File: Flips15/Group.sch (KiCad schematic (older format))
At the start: 6 parts, among them U301 74238, U302 ULN2803/2003, U303 74238, U304 TD62783

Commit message: adding support for optional COM pin at BRDIC1
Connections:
- net GND: no longer U302.1 (I1), U304.1 (I1)
- new net CTLCOMH: U304.1 (I1)
- new net CTLCOML: U302.1 (I1)
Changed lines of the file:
@@
 AR Path="/5C4DA960/5C4DAAA8/5C4CE34D" Ref="U1004"  Part="1"
 AR Path="/5C4DA960/5C4DAABF/5C4CE34D" Ref="U1104"  Part="1"
-F 0 "U804" H 5900 4978 50  0000 C CNN
+F 0 "U1104" H 5900 4978 50  0000 C CNN
 F 1 "TD62783" H 5900 4887 50  0000 C CNN
 F 2 "Housings_DIP:DIP-18_W7.62mm_Socket" H 5900 3750 50  0001 C CNN
@@
 AR Path="/5C4DA960/5C4DAAA8/5C4CE354" Ref="U1001"  Part="1"
 AR Path="/5C4DA960/5C4DAABF/5C4CE354" Ref="U1101"  Part="1"
-F 0 "U801" H 4550 2116 50  0000 C CNN
+F 0 "U1101" H 4550 2116 50  0000 C CNN
 F 1 "74238" H 4550 2025 50  0000 C CNN
 F 2 "Housings_SOIC:SOIC-16_3.9x9.9mm_Pitch1.27mm" H 4550 1600 50  0001 C CNN
@@
 AR Path="/5C4DA960/5C4DAAA8/5C4CE35B" Ref="U1003"  Part="1"
 AR Path="/5C4DA960/5C4DAABF/5C4CE35B" Ref="U1103"  Part="1"
-F 0 "U803" H 4550 4716 50  0000 C CNN
+F 0 "U1103" H 4550 4716 50  0000 C CNN
 F 1 "74238" H 4550 4625 50  0000 C CNN
 F 2 "Housings_SOIC:SOIC-16_3.9x9.9mm_Pitch1.27mm" H 4550 4200 50  0001 C CNN
@@
 AR Path="/5C4DA960/5C4DAAA8/5C4D1DBE" Ref="#PWR01006"  Part="1"
 AR Path="/5C4DA960/5C4DAABF/5C4D1DBE" Ref="#PWR01106"  Part="1"
-F 0 "#PWR0806" H 5900 2350 50  0001 C CNN
+F 0 "#PWR01106" H 5900 2350 50  0001 C CNN
 F 1 "GND" H 5905 2427 50  0000 C CNN
 F 2 "" H 5900 2600 50  0001 C CNN
@@
 AR Path="/5C4DA960/5C4DAAA8/5C4D1DFA" Ref="#PWR01012"  Part="1"
 AR Path="/5C4DA960/5C4DAABF/5C4D1DFA" Ref="#PWR01112"  Part="1"
-F 0 "#PWR0812" H 5900 5050 50  0001 C CNN
+F 0 "#PWR01112" H 5900 5050 50  0001 C CNN
 F 1 "GND" H 5905 5127 50  0000 C CNN
 F 2 "" H 5900 5300 50  0001 C CNN
@@
 AR Path="/5C4DA960/5C4DAAA8/5C4D1E20" Ref="#PWR01011"  Part="1"
 AR Path="/5C4DA960/5C4DAABF/5C4D1E20" Ref="#PWR01111"  Part="1"
-F 0 "#PWR0811" H 4550 5050 50  0001 C CNN
+F 0 "#PWR01111" H 4550 5050 50  0001 C CNN
 F 1 "GND" H 4555 5127 50  0000 C CNN
 F 2 "" H 4550 5300 50  0001 C CNN
@@
 AR Path="/5C4DA960/5C4DAAA8/5C4D1E50" Ref="#PWR01005"  Part="1"
 AR Path="/5C4DA960/5C4DAABF/5C4D1E50" Ref="#PWR01105"  Part="1"
-F 0 "#PWR0805" H 4550 2350 50  0001 C CNN
+F 0 "#PWR01105" H 4550 2350 50  0001 C CNN
 F 1 "GND" H 4555 2427 50  0000 C CNN
 F 2 "" H 4550 2600 50  0001 C CNN
@@
 AR Path="/5C4DA960/5C4DAAA8/5C4D1F03" Ref="#PWR01002"  Part="1"
 AR Path="/5C4DA960/5C4DAABF/5C4D1F03" Ref="#PWR01102"  Part="1"
-F 0 "#PWR0802" H 6400 600 50  0001 C CNN
+F 0 "#PWR01102" H 6400 600 50  0001 C CNN
 F 1 "+24V" H 6415 923 50  0000 C CNN
 F 2 "" H 6400 750 50  0001 C CNN
@@
 AR Path="/5C4DA960/5C4DAAA8/5C4D1F1D" Ref="#PWR01008"  Part="1"
 AR Path="/5C4DA960/5C4DAABF/5C4D1F1D" Ref="#PWR01108"  Part="1"
-F 0 "#PWR0808" H 5900 3250 50  0001 C CNN
+F 0 "#PWR01108" H 5900 3250 50  0001 C CNN
 F 1 "+24V" H 5915 3573 50  0000 C CNN
 F 2 "" H 5900 3400 50  0001 C CNN
@@
 AR Path="/5C4DA960/5C4DAAA8/5C4D1FAA" Ref="#PWR01001"  Part="1"
 AR Path="/5C4DA960/5C4DAABF/5C4D1FAA" Ref="#PWR01101"  Part="1"
-F 0 "#PWR0801" H 4550 600 50  0001 C CNN
+F 0 "#PWR01101" H 4550 600 50  0001 C CNN
 F 1 "VCC" H 4567 923 50  0000 C CNN
 F 2 "" H 4550 750 50  0001 C CNN
@@
 AR Path="/5C4DA960/5C4DAAA8/5C4D1FD4" Ref="#PWR01007"  Part="1"
 AR Path="/5C4DA960/5C4DAABF/5C4D1FD4" Ref="#PWR01107"  Part="1"
-F 0 "#PWR0807" H 4550 3250 50  0001 C CNN
+F 0 "#PWR01107" H 4550 3250 50  0001 C CNN
 F 1 "VCC" H 4567 3573 50  0000 C CNN
 F 2 "" H 4550 3400 50  0001 C CNN
@@
 AR Path="/5C4DA960/5C4DAAA8/5C4DA0A7" Ref="#PWR01010"  Part="1"
 AR Path="/5C4DA960/5C4DAABF/5C4DA0A7" Ref="#PWR01110"  Part="1"
-F 0 "#PWR0810" H 3900 3900 50  0001 C CNN
+F 0 "#PWR01110" H 3900 3900 50  0001 C CNN
 F 1 "GND" V 3905 4022 50  0000 R CNN
 F 2 "" H 3900 4150 50  0001 C CNN
@@
 AR Path="/5C4DA960/5C4DAAA8/5C4E1AEA" Ref="U1002"  Part="1"
 AR Path="/5C4DA960/5C4DAABF/5C4E1AEA" Ref="U1102"  Part="1"
-F 0 "U802" H 5900 2167 50  0000 C CNN
+F 0 "U1102" H 5900 2167 50  0000 C CNN
 F 1 "ULN2803/2003" H 5900 2076 50  0000 C CNN
 F 2 "Housings_DIP:DIP-18_W7.62mm_Socket" H 5950 950 50  0001 L CNN
@@
 AR Path="/5C4DA960/5C4DAAA8/5C4F67EE" Ref="C1002"  Part="1"
 AR Path="/5C4DA960/5C4DAABF/5C4F67EE" Ref="C1102"  Part="1"
-F 0 "C802" V 4021 3500 50  0000 C CNN
+F 0 "C1102" V 4021 3500 50  0000 C CNN
 F 1 "0μ1" V 4112 3500 50  0000 C CNN
 F 2 "Capacitors_SMD:C_0805_HandSoldering" H 4250 3500 50  0001 C CNN
@@
 AR Path="/5C4DA960/5C4DAAA8/5C4F6885" Ref="C1001"  Part="1"
 AR Path="/5C4DA960/5C4DAABF/5C4F6885" Ref="C1101"  Part="1"
-F 0 "C801" V 4021 850 50  0000 C CNN
+F 0 "C1101" V 4021 850 50  0000 C CNN
 F 1 "0μ1" V 4112 850 50  0000 C CNN
 F 2 "Capacitors_SMD:C_0805_HandSoldering" H 4250 850 50  0001 C CNN
@@
 AR Path="/5C4DA960/5C4DAAA8/5C4F6943" Ref="#PWR01003"  Part="1"
 AR Path="/5C4DA960/5C4DAABF/5C4F6943" Ref="#PWR01103"  Part="1"
-F 0 "#PWR0803" H 3900 600 50  0001 C CNN
+F 0 "#PWR01103" H 3900 600 50  0001 C CNN
 F 1 "GND" V 3905 722 50  0000 R CNN
 F 2 "" H 3900 850 50  0001 C CNN
@@
 AR Path="/5C4DA960/5C4DAAA8/5C4F6978" Ref="#PWR01009"  Part="1"
 AR Path="/5C4DA960/5C4DAABF/5C4F6978" Ref="#PWR01109"  Part="1"
-F 0 "#PWR0809" H 3900 3250 50  0001 C CNN
+F 0 "#PWR01109" H 3900 3250 50  0001 C CNN
 F 1 "GND" V 3905 3372 50  0000 R CNN
 F 2 "" H 3900 3500 50  0001 C CNN
@@
 AR Path="/5C4DA960/5C4DAAA8/5C4EB0F4" Ref="#PWR0130"  Part="1"
 AR Path="/5C4DA960/5C4DAABF/5C4EB0F4" Ref="#PWR0133"  Part="1"
-F 0 "#PWR0124" H 3900 3750 50  0001 C CNN
+F 0 "#PWR0133" H 3900 3750 50  0001 C CNN
 F 1 "GND" V 3905 3872 50  0000 R CNN
 F 2 "" H 3900 4000 50  0001 C CNN
@@
 AR Path="/5C4DA960/5C4DAAA8/5C4EC62E" Ref="#PWR0131"  Part="1"
 AR Path="/5C4DA960/5C4DAABF/5C4EC62E" Ref="#PWR0134"  Part="1"
-F 0 "#PWR0125" H 3900 1150 50  0001 C CNN
+F 0 "#PWR0134" H 3900 1150 50  0001 C CNN
 F 1 "GND" V 3905 1272 50  0000 R CNN
 F 2 "" H 3900 1400 50  0001 C CNN
@@
 AR Path="/5C4DA960/5C4DAAA8/5C4EC645" Ref="#PWR0132"  Part="1"
 AR Path="/5C4DA960/5C4DAABF/5C4EC645" Ref="#PWR0135"  Part="1"
-F 0 "#PWR0126" H 3900 1300 50  0001 C CNN
+F 0 "#PWR0135" H 3900 1300 50  0001 C CNN
 F 1 "GND" V 3905 1422 50  0000 R CNN
 F 2 "" H 3900 1550 50  0001 C CNN
@@
 NoConn ~ 5100 1400
 NoConn ~ 5100 4000
-$Comp
-L power:GND #PWR?
-U 1 1 5C57C882
-P 5500 1400
-AR Path="/5C4DA960/5C4DAA7A/5C57C882" Ref="#PWR?"  Part="1"
-AR Path="/5C4DA960/5C4DAA91/5C57C882" Ref="#PWR?"  Part="1"
-AR Path="/5C4DA960/5C4DAAA8/5C57C882" Ref="#PWR?"  Part="1"
-AR Path="/5C4DA960/5C4DAABF/5C57C882" Ref="#PWR?"  Part="1"
-F 0 "#PWR?" H 5500 1150 50  0001 C CNN
-F 1 "GND" V 5505 1272 50  0000 R CNN
-F 2 "" H 5500 1400 50  0001 C CNN
-F 3 "" H 5500 1400 50  0001 C CNN
-	1    5500 1400
-	0    1    1    0
-$EndComp
-$Comp
-L power:GND #PWR?
-U 1 1 5C57C8A6
-P 5500 4000
-AR Path="/5C4DA960/5C4DAA7A/5C57C8A6" Ref="#PWR?"  Part="1"
-AR Path="/5C4DA960/5C4DAA91/5C57C8A6" Ref="#PWR?"  Part="1"
-AR Path="/5C4DA960/5C4DAAA8/5C57C8A6" Ref="#PWR?"  Part="1"
-AR Path="/5C4DA960/5C4DAABF/5C57C8A6" Ref="#PWR?"  Part="1"
-F 0 "#PWR?" H 5500 3750 50  0001 C CNN
-F 1 "GND" V 5505 3872 50  0000 R CNN
-F 2 "" H 5500 4000 50  0001 C CNN
-F 3 "" H 5500 4000 50  0001 C CNN
-	1    5500 4000
-	0    1    1    0
-$EndComp
+Text HLabel 5250 850  0    50   Input ~ 0
+CTLCOML
+Wire Wire Line
+	5500 1400 5400 1400
+Wire Wire Line
+	5400 1400 5400 850
+Wire Wire Line
+	5400 850  5250 850
+Text HLabel 5250 3500 0    50   Input ~ 0
+CTLCOMH
+Wire Wire Line
+	5250 3500 5400 3500
+Wire Wire Line
+	5400 3500 5400 4000
+Wire Wire Line
+	5400 4000 5500 4000
 $EndSCHEMATC

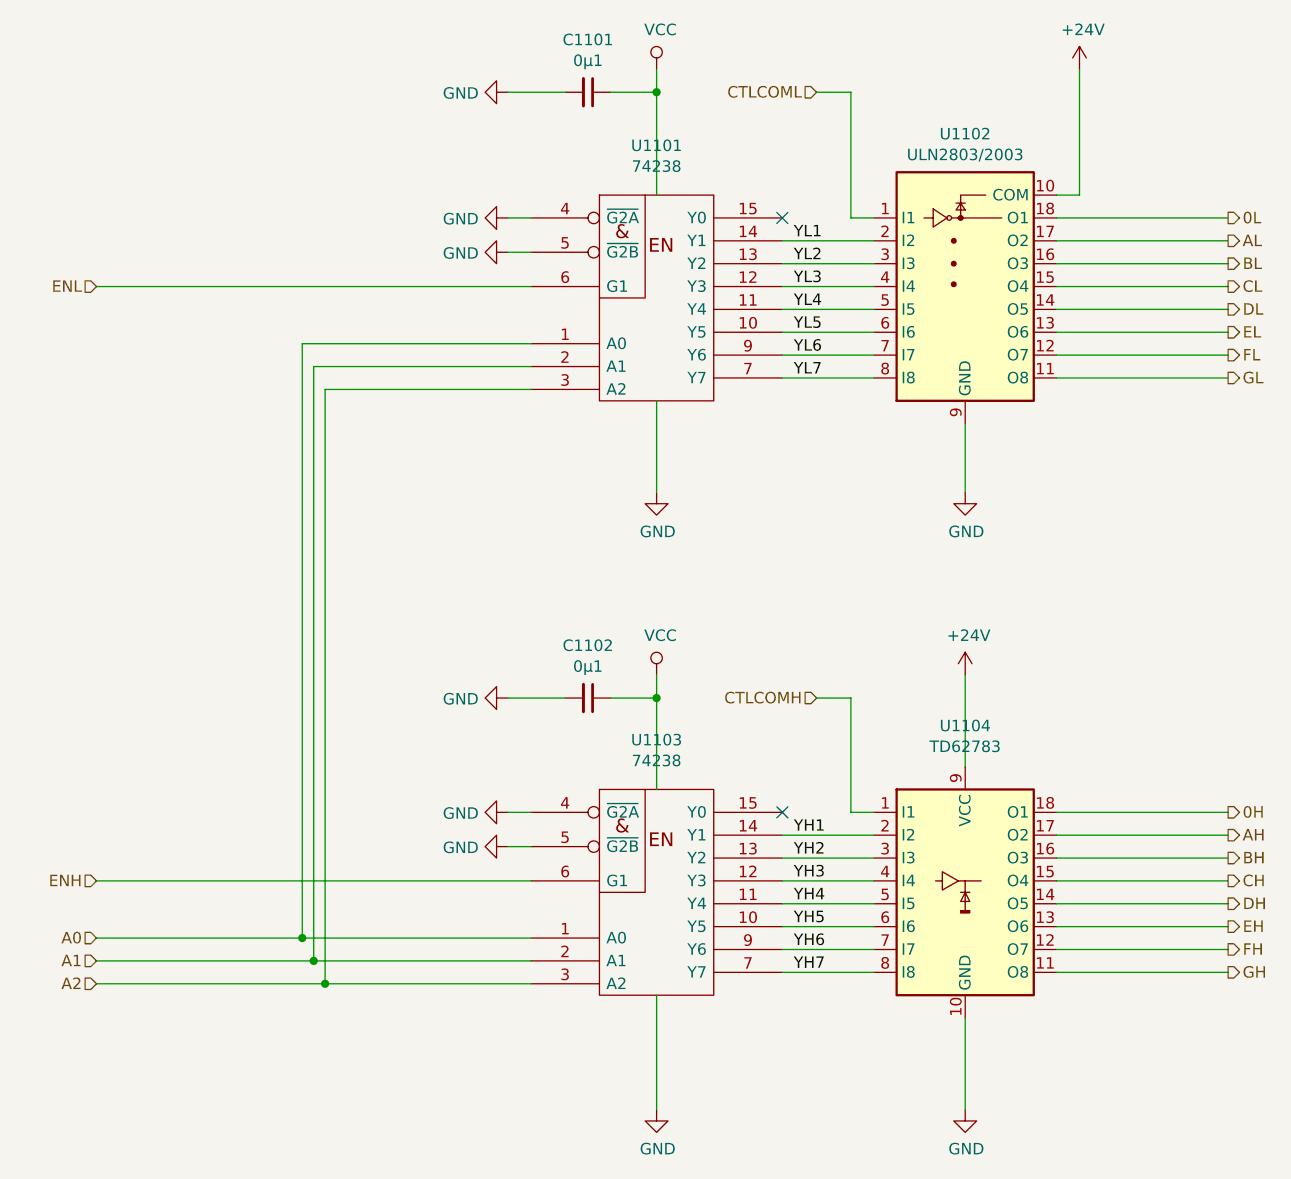
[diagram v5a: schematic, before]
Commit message: re-annotating to get more compact part numbers
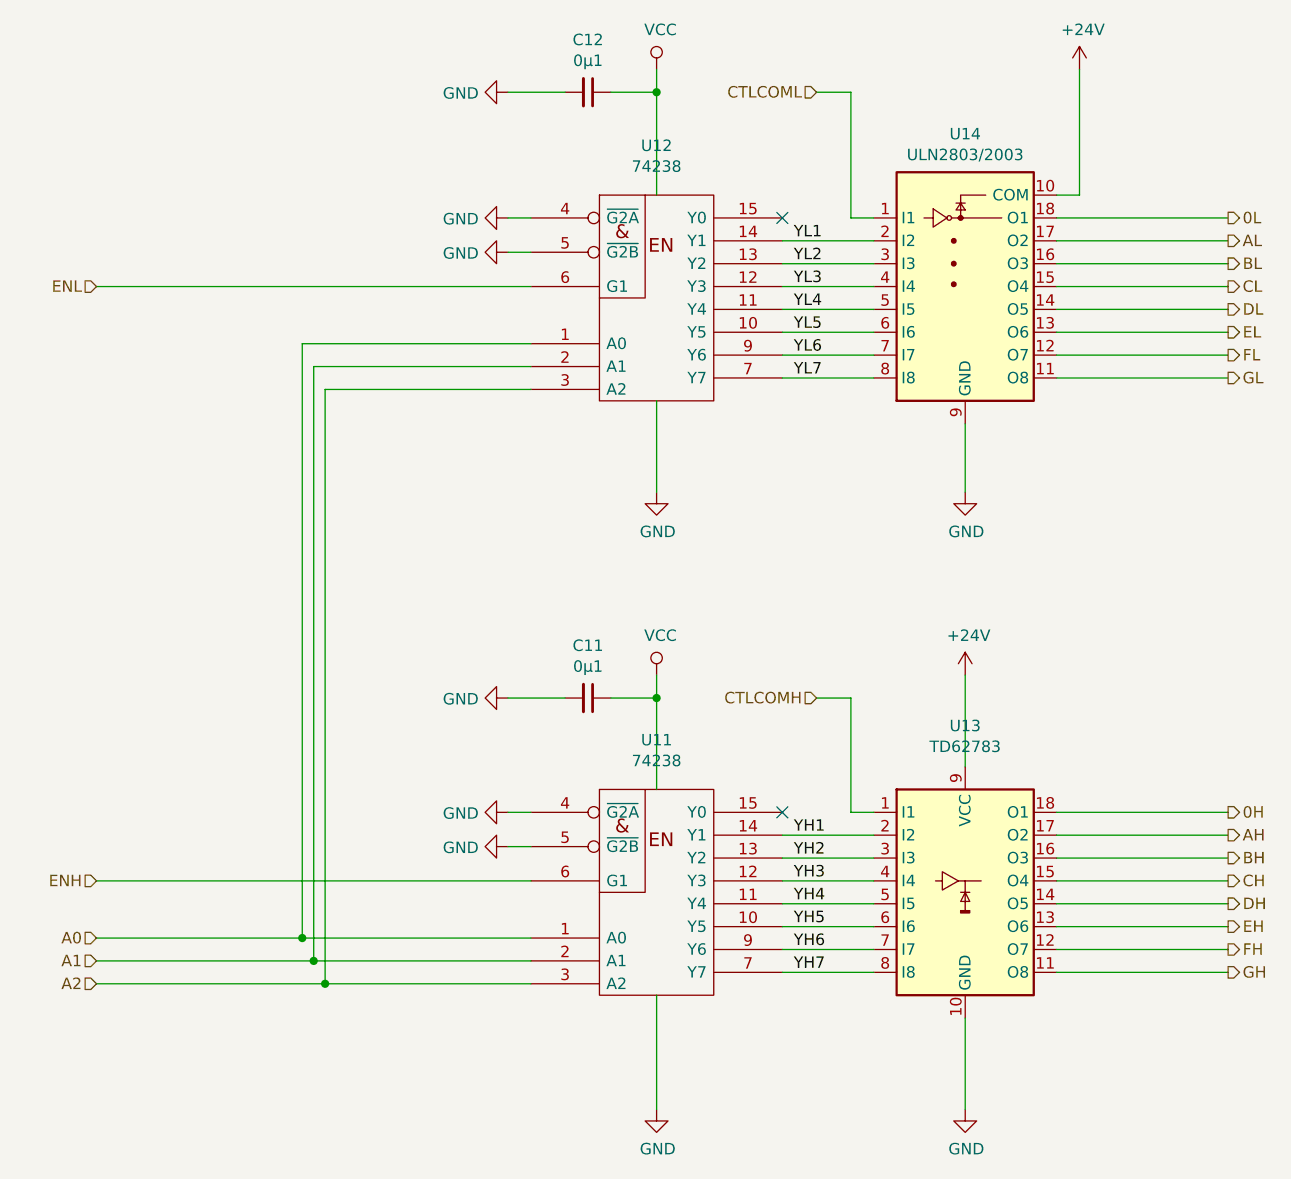
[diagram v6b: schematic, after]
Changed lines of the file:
@@
 AR Path="/5C4DA950/5C4DAAA8/5C4CE34D" Ref="U504"  Part="1"
 AR Path="/5C4DA950/5C4DAABF/5C4CE34D" Ref="U604"  Part="1"
-AR Path="/5C4DA960/5C4DAA7A/5C4CE34D" Ref="U804"  Part="1"
-AR Path="/5C4DA960/5C4DAA91/5C4CE34D" Ref="U904"  Part="1"
-AR Path="/5C4DA960/5C4DAAA8/5C4CE34D" Ref="U1004"  Part="1"
-AR Path="/5C4DA960/5C4DAABF/5C4CE34D" Ref="U1104"  Part="1"
-F 0 "U1104" H 5900 4978 50  0000 C CNN
+AR Path="/5C4DA960/5C4DAA7A/5C4CE34D" Ref="U13"  Part="1"
+AR Path="/5C4DA960/5C4DAA91/5C4CE34D" Ref="U23"  Part="1"
+AR Path="/5C4DA960/5C4DAAA8/5C4CE34D" Ref="U33"  Part="1"
+AR Path="/5C4DA960/5C4DAABF/5C4CE34D" Ref="U43"  Part="1"
+F 0 "U13" H 5900 4978 50  0000 C CNN
 F 1 "TD62783" H 5900 4887 50  0000 C CNN
 F 2 "Housings_DIP:DIP-18_W7.62mm_Socket" H 5900 3750 50  0001 C CNN
@@
 AR Path="/5C4DA950/5C4DAAA8/5C4CE354" Ref="U501"  Part="1"
 AR Path="/5C4DA950/5C4DAABF/5C4CE354" Ref="U601"  Part="1"
-AR Path="/5C4DA960/5C4DAA7A/5C4CE354" Ref="U801"  Part="1"
-AR Path="/5C4DA960/5C4DAA91/5C4CE354" Ref="U901"  Part="1"
-AR Path="/5C4DA960/5C4DAAA8/5C4CE354" Ref="U1001"  Part="1"
-AR Path="/5C4DA960/5C4DAABF/5C4CE354" Ref="U1101"  Part="1"
-F 0 "U1101" H 4550 2116 50  0000 C CNN
+AR Path="/5C4DA960/5C4DAA7A/5C4CE354" Ref="U12"  Part="1"
+AR Path="/5C4DA960/5C4DAA91/5C4CE354" Ref="U22"  Part="1"
+AR Path="/5C4DA960/5C4DAAA8/5C4CE354" Ref="U32"  Part="1"
+AR Path="/5C4DA960/5C4DAABF/5C4CE354" Ref="U42"  Part="1"
+F 0 "U12" H 4550 2116 50  0000 C CNN
 F 1 "74238" H 4550 2025 50  0000 C CNN
 F 2 "Housings_SOIC:SOIC-16_3.9x9.9mm_Pitch1.27mm" H 4550 1600 50  0001 C CNN
@@
 AR Path="/5C4DA950/5C4DAAA8/5C4CE35B" Ref="U503"  Part="1"
 AR Path="/5C4DA950/5C4DAABF/5C4CE35B" Ref="U603"  Part="1"
-AR Path="/5C4DA960/5C4DAA7A/5C4CE35B" Ref="U803"  Part="1"
-AR Path="/5C4DA960/5C4DAA91/5C4CE35B" Ref="U903"  Part="1"
-AR Path="/5C4DA960/5C4DAAA8/5C4CE35B" Ref="U1003"  Part="1"
-AR Path="/5C4DA960/5C4DAABF/5C4CE35B" Ref="U1103"  Part="1"
-F 0 "U1103" H 4550 4716 50  0000 C CNN
+AR Path="/5C4DA960/5C4DAA7A/5C4CE35B" Ref="U11"  Part="1"
+AR Path="/5C4DA960/5C4DAA91/5C4CE35B" Ref="U21"  Part="1"
+AR Path="/5C4DA960/5C4DAAA8/5C4CE35B" Ref="U31"  Part="1"
+AR Path="/5C4DA960/5C4DAABF/5C4CE35B" Ref="U41"  Part="1"
+F 0 "U11" H 4550 4716 50  0000 C CNN
 F 1 "74238" H 4550 4625 50  0000 C CNN
 F 2 "Housings_SOIC:SOIC-16_3.9x9.9mm_Pitch1.27mm" H 4550 4200 50  0001 C CNN
@@
 AR Path="/5C4DA960/5C4DAAA8/5C4D1DBE" Ref="#PWR01006"  Part="1"
 AR Path="/5C4DA960/5C4DAABF/5C4D1DBE" Ref="#PWR01106"  Part="1"
-F 0 "#PWR01106" H 5900 2350 50  0001 C CNN
+F 0 "#PWR0806" H 5900 2350 50  0001 C CNN
 F 1 "GND" H 5905 2427 50  0000 C CNN
 F 2 "" H 5900 2600 50  0001 C CNN
@@
 AR Path="/5C4DA960/5C4DAAA8/5C4D1DFA" Ref="#PWR01012"  Part="1"
 AR Path="/5C4DA960/5C4DAABF/5C4D1DFA" Ref="#PWR01112"  Part="1"
-F 0 "#PWR01112" H 5900 5050 50  0001 C CNN
+F 0 "#PWR0812" H 5900 5050 50  0001 C CNN
 F 1 "GND" H 5905 5127 50  0000 C CNN
 F 2 "" H 5900 5300 50  0001 C CNN
@@
 AR Path="/5C4DA960/5C4DAAA8/5C4D1E20" Ref="#PWR01011"  Part="1"
 AR Path="/5C4DA960/5C4DAABF/5C4D1E20" Ref="#PWR01111"  Part="1"
-F 0 "#PWR01111" H 4550 5050 50  0001 C CNN
+F 0 "#PWR0811" H 4550 5050 50  0001 C CNN
 F 1 "GND" H 4555 5127 50  0000 C CNN
 F 2 "" H 4550 5300 50  0001 C CNN
@@
 AR Path="/5C4DA960/5C4DAAA8/5C4D1E50" Ref="#PWR01005"  Part="1"
 AR Path="/5C4DA960/5C4DAABF/5C4D1E50" Ref="#PWR01105"  Part="1"
-F 0 "#PWR01105" H 4550 2350 50  0001 C CNN
+F 0 "#PWR0805" H 4550 2350 50  0001 C CNN
 F 1 "GND" H 4555 2427 50  0000 C CNN
 F 2 "" H 4550 2600 50  0001 C CNN
@@
 AR Path="/5C4DA960/5C4DAAA8/5C4D1F03" Ref="#PWR01002"  Part="1"
 AR Path="/5C4DA960/5C4DAABF/5C4D1F03" Ref="#PWR01102"  Part="1"
-F 0 "#PWR01102" H 6400 600 50  0001 C CNN
+F 0 "#PWR0802" H 6400 600 50  0001 C CNN
 F 1 "+24V" H 6415 923 50  0000 C CNN
 F 2 "" H 6400 750 50  0001 C CNN
@@
 AR Path="/5C4DA960/5C4DAAA8/5C4D1F1D" Ref="#PWR01008"  Part="1"
 AR Path="/5C4DA960/5C4DAABF/5C4D1F1D" Ref="#PWR01108"  Part="1"
-F 0 "#PWR01108" H 5900 3250 50  0001 C CNN
+F 0 "#PWR0808" H 5900 3250 50  0001 C CNN
 F 1 "+24V" H 5915 3573 50  0000 C CNN
 F 2 "" H 5900 3400 50  0001 C CNN
@@
 AR Path="/5C4DA960/5C4DAAA8/5C4D1FAA" Ref="#PWR01001"  Part="1"
 AR Path="/5C4DA960/5C4DAABF/5C4D1FAA" Ref="#PWR01101"  Part="1"
-F 0 "#PWR01101" H 4550 600 50  0001 C CNN
+F 0 "#PWR0801" H 4550 600 50  0001 C CNN
 F 1 "VCC" H 4567 923 50  0000 C CNN
 F 2 "" H 4550 750 50  0001 C CNN
@@
 AR Path="/5C4DA960/5C4DAAA8/5C4D1FD4" Ref="#PWR01007"  Part="1"
 AR Path="/5C4DA960/5C4DAABF/5C4D1FD4" Ref="#PWR01107"  Part="1"
-F 0 "#PWR01107" H 4550 3250 50  0001 C CNN
+F 0 "#PWR0807" H 4550 3250 50  0001 C CNN
 F 1 "VCC" H 4567 3573 50  0000 C CNN
 F 2 "" H 4550 3400 50  0001 C CNN
@@
 AR Path="/5C4DA960/5C4DAAA8/5C4DA0A7" Ref="#PWR01010"  Part="1"
 AR Path="/5C4DA960/5C4DAABF/5C4DA0A7" Ref="#PWR01110"  Part="1"
-F 0 "#PWR01110" H 3900 3900 50  0001 C CNN
+F 0 "#PWR0810" H 3900 3900 50  0001 C CNN
 F 1 "GND" V 3905 4022 50  0000 R CNN
 F 2 "" H 3900 4150 50  0001 C CNN
@@
 AR Path="/5C4DA950/5C4DAAA8/5C4E1AEA" Ref="U502"  Part="1"
 AR Path="/5C4DA950/5C4DAABF/5C4E1AEA" Ref="U602"  Part="1"
-AR Path="/5C4DA960/5C4DAA7A/5C4E1AEA" Ref="U802"  Part="1"
-AR Path="/5C4DA960/5C4DAA91/5C4E1AEA" Ref="U902"  Part="1"
-AR Path="/5C4DA960/5C4DAAA8/5C4E1AEA" Ref="U1002"  Part="1"
-AR Path="/5C4DA960/5C4DAABF/5C4E1AEA" Ref="U1102"  Part="1"
-F 0 "U1102" H 5900 2167 50  0000 C CNN
+AR Path="/5C4DA960/5C4DAA7A/5C4E1AEA" Ref="U14"  Part="1"
+AR Path="/5C4DA960/5C4DAA91/5C4E1AEA" Ref="U24"  Part="1"
+AR Path="/5C4DA960/5C4DAAA8/5C4E1AEA" Ref="U34"  Part="1"
+AR Path="/5C4DA960/5C4DAABF/5C4E1AEA" Ref="U44"  Part="1"
+F 0 "U14" H 5900 2167 50  0000 C CNN
 F 1 "ULN2803/2003" H 5900 2076 50  0000 C CNN
 F 2 "Housings_DIP:DIP-18_W7.62mm_Socket" H 5950 950 50  0001 L CNN
@@
 AR Path="/5C4DA950/5C4DAAA8/5C4F67EE" Ref="C502"  Part="1"
 AR Path="/5C4DA950/5C4DAABF/5C4F67EE" Ref="C602"  Part="1"
-AR Path="/5C4DA960/5C4DAA7A/5C4F67EE" Ref="C802"  Part="1"
-AR Path="/5C4DA960/5C4DAA91/5C4F67EE" Ref="C902"  Part="1"
-AR Path="/5C4DA960/5C4DAAA8/5C4F67EE" Ref="C1002"  Part="1"
-AR Path="/5C4DA960/5C4DAABF/5C4F67EE" Ref="C1102"  Part="1"
-F 0 "C1102" V 4021 3500 50  0000 C CNN
+AR Path="/5C4DA960/5C4DAA7A/5C4F67EE" Ref="C11"  Part="1"
+AR Path="/5C4DA960/5C4DAA91/5C4F67EE" Ref="C21"  Part="1"
+AR Path="/5C4DA960/5C4DAAA8/5C4F67EE" Ref="C31"  Part="1"
+AR Path="/5C4DA960/5C4DAABF/5C4F67EE" Ref="C41"  Part="1"
+F 0 "C11" V 4021 3500 50  0000 C CNN
 F 1 "0μ1" V 4112 3500 50  0000 C CNN
 F 2 "Capacitors_SMD:C_0805_HandSoldering" H 4250 3500 50  0001 C CNN
@@
 AR Path="/5C4DA950/5C4DAAA8/5C4F6885" Ref="C501"  Part="1"
 AR Path="/5C4DA950/5C4DAABF/5C4F6885" Ref="C601"  Part="1"
-AR Path="/5C4DA960/5C4DAA7A/5C4F6885" Ref="C801"  Part="1"
-AR Path="/5C4DA960/5C4DAA91/5C4F6885" Ref="C901"  Part="1"
-AR Path="/5C4DA960/5C4DAAA8/5C4F6885" Ref="C1001"  Part="1"
-AR Path="/5C4DA960/5C4DAABF/5C4F6885" Ref="C1101"  Part="1"
-F 0 "C1101" V 4021 850 50  0000 C CNN
+AR Path="/5C4DA960/5C4DAA7A/5C4F6885" Ref="C12"  Part="1"
+AR Path="/5C4DA960/5C4DAA91/5C4F6885" Ref="C22"  Part="1"
+AR Path="/5C4DA960/5C4DAAA8/5C4F6885" Ref="C32"  Part="1"
+AR Path="/5C4DA960/5C4DAABF/5C4F6885" Ref="C42"  Part="1"
+F 0 "C12" V 4021 850 50  0000 C CNN
 F 1 "0μ1" V 4112 850 50  0000 C CNN
 F 2 "Capacitors_SMD:C_0805_HandSoldering" H 4250 850 50  0001 C CNN
@@
 AR Path="/5C4DA960/5C4DAAA8/5C4F6943" Ref="#PWR01003"  Part="1"
 AR Path="/5C4DA960/5C4DAABF/5C4F6943" Ref="#PWR01103"  Part="1"
-F 0 "#PWR01103" H 3900 600 50  0001 C CNN
+F 0 "#PWR0803" H 3900 600 50  0001 C CNN
 F 1 "GND" V 3905 722 50  0000 R CNN
 F 2 "" H 3900 850 50  0001 C CNN
@@
 AR Path="/5C4DA960/5C4DAAA8/5C4F6978" Ref="#PWR01009"  Part="1"
 AR Path="/5C4DA960/5C4DAABF/5C4F6978" Ref="#PWR01109"  Part="1"
-F 0 "#PWR01109" H 3900 3250 50  0001 C CNN
+F 0 "#PWR0809" H 3900 3250 50  0001 C CNN
 F 1 "GND" V 3905 3372 50  0000 R CNN
 F 2 "" H 3900 3500 50  0001 C CNN
@@
 AR Path="/5C4DA960/5C4DAAA8/5C4EB0F4" Ref="#PWR0130"  Part="1"
 AR Path="/5C4DA960/5C4DAABF/5C4EB0F4" Ref="#PWR0133"  Part="1"
-F 0 "#PWR0133" H 3900 3750 50  0001 C CNN
+F 0 "#PWR0124" H 3900 3750 50  0001 C CNN
 F 1 "GND" V 3905 3872 50  0000 R CNN
 F 2 "" H 3900 4000 50  0001 C CNN
@@
 AR Path="/5C4DA960/5C4DAAA8/5C4EC62E" Ref="#PWR0131"  Part="1"
 AR Path="/5C4DA960/5C4DAABF/5C4EC62E" Ref="#PWR0134"  Part="1"
-F 0 "#PWR0134" H 3900 1150 50  0001 C CNN
+F 0 "#PWR0125" H 3900 1150 50  0001 C CNN
 F 1 "GND" V 3905 1272 50  0000 R CNN
 F 2 "" H 3900 1400 50  0001 C CNN
@@
 AR Path="/5C4DA960/5C4DAAA8/5C4EC645" Ref="#PWR0132"  Part="1"
 AR Path="/5C4DA960/5C4DAABF/5C4EC645" Ref="#PWR0135"  Part="1"
-F 0 "#PWR0135" H 3900 1300 50  0001 C CNN
+F 0 "#PWR0126" H 3900 1300 50  0001 C CNN
 F 1 "GND" V 3905 1422 50  0000 R CNN
 F 2 "" H 3900 1550 50  0001 C CNN
